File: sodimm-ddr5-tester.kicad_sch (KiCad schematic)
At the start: 2 parts

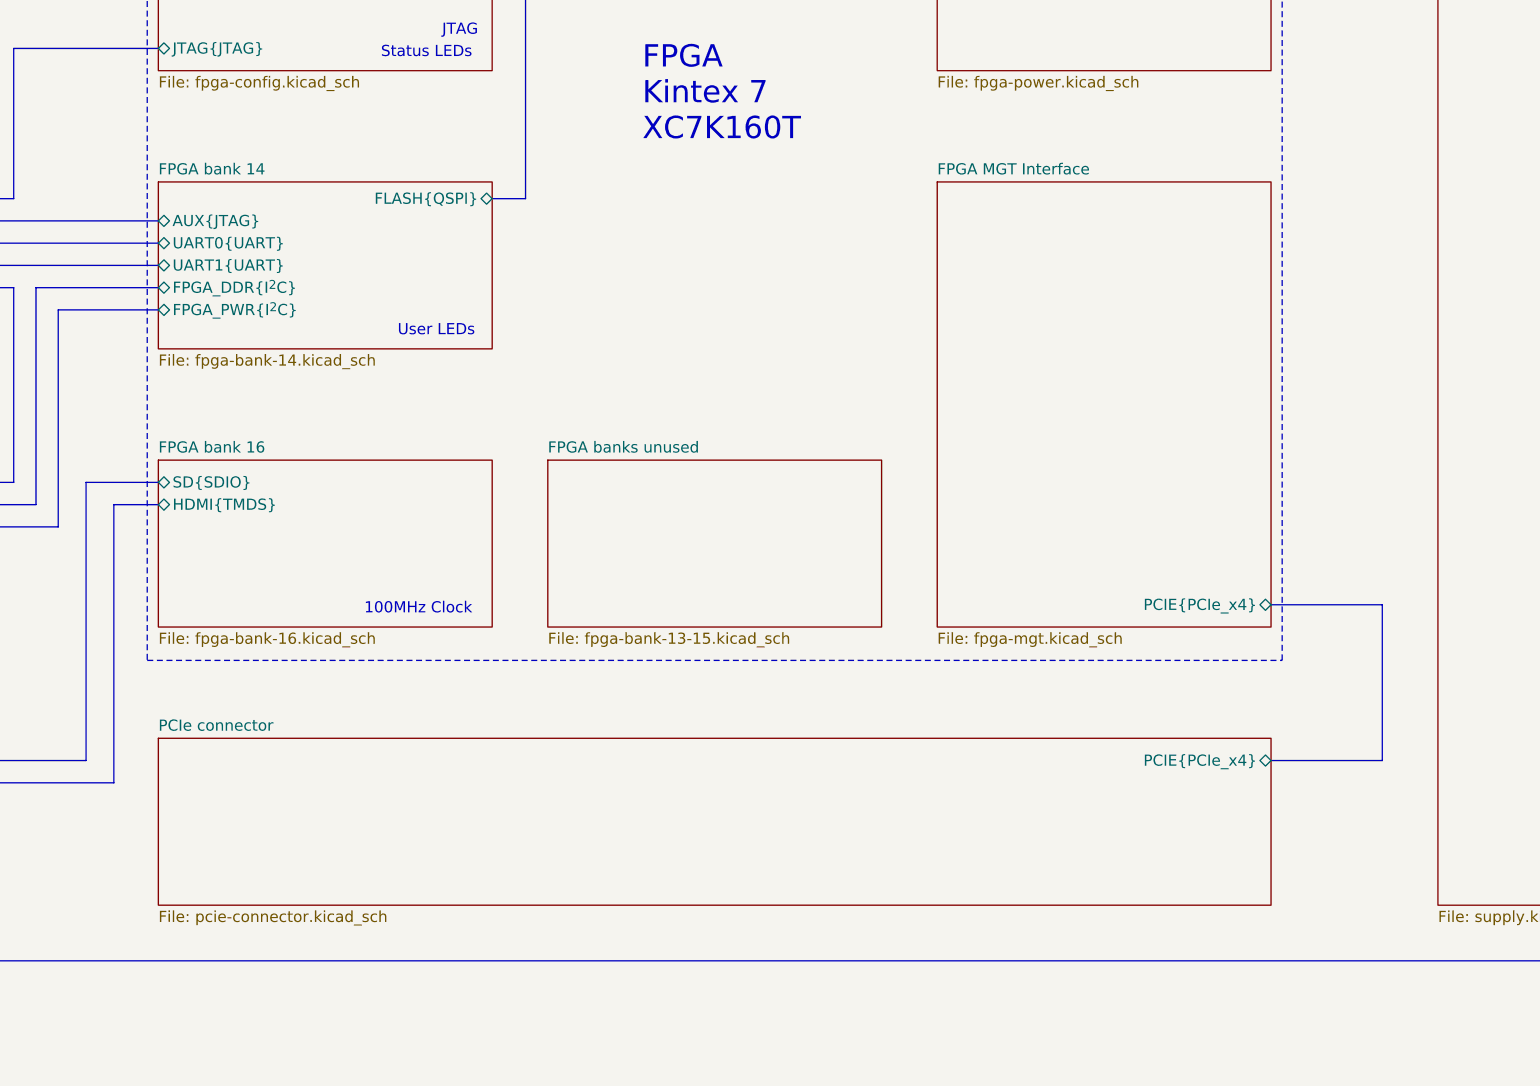
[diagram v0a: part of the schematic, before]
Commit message: Removing PCIe from sch and PCB
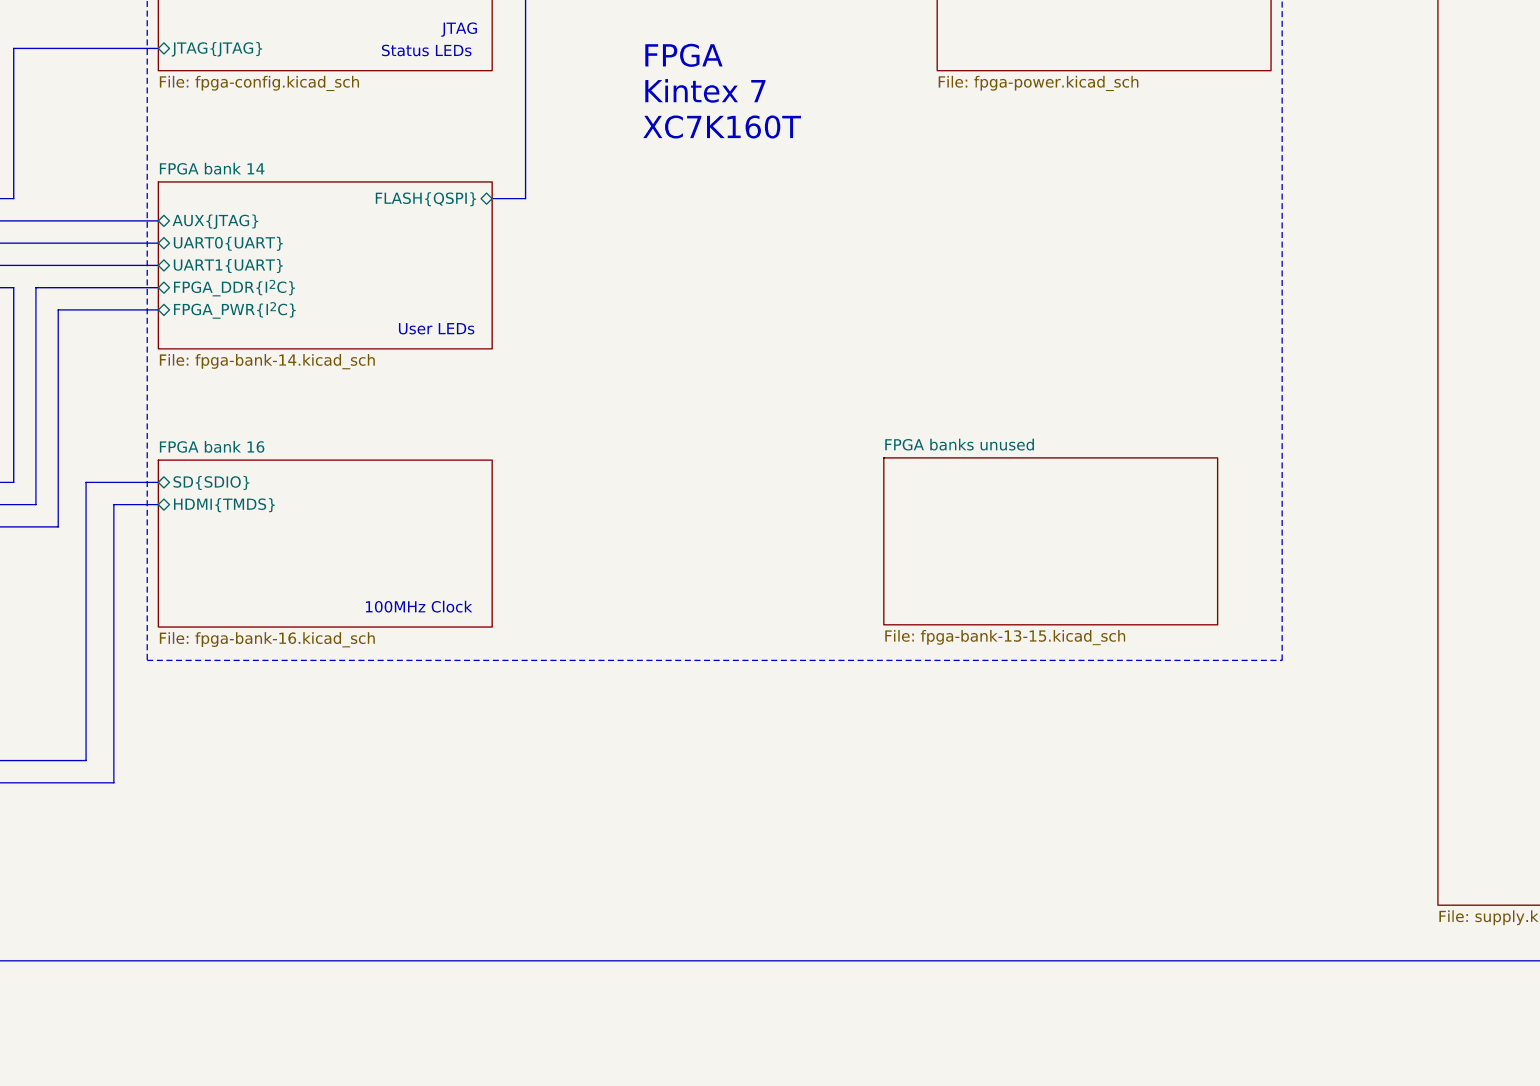
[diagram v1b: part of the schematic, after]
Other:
- removed sheet FPGA MGT Interface
- removed sheet PCIe connector
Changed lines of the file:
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@@
-    (stroke (width 0) (type default))
-  )
-  (bus (pts (xy 285.75 212.09) (xy 273.05 212.09))
     (stroke (width 0) (type default))
   )
@@
     (stroke (width 0) (type default))
   )
-  (bus (pts (xy 273.05 194.31) (xy 285.75 194.31))
-    (stroke (width 0) (type default))
-  )
   (bus (pts (xy 140.97 214.63) (xy 127 214.63))
     (stroke (width 0) (type default))
@@
   )
   (bus (pts (xy 281.94 62.865) (xy 273.05 62.865))
-    (stroke (width 0) (type default))
-  )
-  (bus (pts (xy 285.75 194.31) (xy 285.75 212.09))
     (stroke (width 0) (type default))
   )
@@
     )
   )
-  (sheet (at 190.5 177.8) (size 38.1 19.05) (fields_autoplaced)
+  (sheet (at 228.854 177.546) (size 38.1 19.05) (fields_autoplaced)
     (stroke (width 0.1524) (type solid))
     (fill (color 0 0 0 0.0000))
-    (property "Sheetname" "FPGA banks unused" (at 190.5 177.0884 0)
+    (property "Sheetname" "FPGA banks unused" (at 228.854 176.8344 0)
       (effects (font (size 1.27 1.27)) (justify left bottom))
     )
-    (property "Sheetfile" "fpga-bank-13-15.kicad_sch" (at 190.5 197.4346 0)
+    (property "Sheetfile" "fpga-bank-13-15.kicad_sch" (at 228.854 197.1806 0)
       (effects (font (size 1.27 1.27)) (justify left top))
     )
@@
       )
     )
-  )
-  (sheet (at 234.95 146.05) (size 38.1 50.8) (fields_autoplaced)
-    (stroke (width 0.1524) (type solid))
-    (fill (color 0 0 0 0.0000))
-    (property "Sheetname" "FPGA MGT Interface" (at 234.95 145.3384 0)
-      (effects (font (size 1.27 1.27)) (justify left bottom))
-    )
-    (property "Sheetfile" "fpga-mgt.kicad_sch" (at 234.95 197.4346 0)
-      (effects (font (size 1.27 1.27)) (justify left top))
-    )
-    (pin "PCIE{PCIe_x4}" bidirectional (at 273.05 194.31 0)
-      (effects (font (size 1.27 1.27)) (justify right))
-    )
-    (instances
-      (project "sodimm-ddr5-tester"
-        (path "/1faa6543-e26a-4449-8bac-ee14b9f19e5f" (page "11"))
-      )
-    )
-  )
-  (sheet (at 146.05 209.55) (size 127 19.05) (fields_autoplaced)
-    (stroke (width 0.1524) (type solid))
-    (fill (color 0 0 0 0.0000))
-    (property "Sheetname" "PCIe connector" (at 146.05 208.8384 0)
-      (effects (font (size 1.27 1.27)) (justify left bottom))
-    )
-    (property "Sheetfile" "pcie-connector.kicad_sch" (at 146.05 229.1846 0)
-      (effects (font (size 1.27 1.27)) (justify left top))
-    )
-    (pin "PCIE{PCIe_x4}" tri_state (at 273.05 212.09 0)
-      (effects (font (size 1.27 1.27)) (justify right))
-    )
-    (instances
-      (project "sodimm-ddr5-tester"
-        (path "/1faa6543-e26a-4449-8bac-ee14b9f19e5f" (page "12"))
-      )
-    )

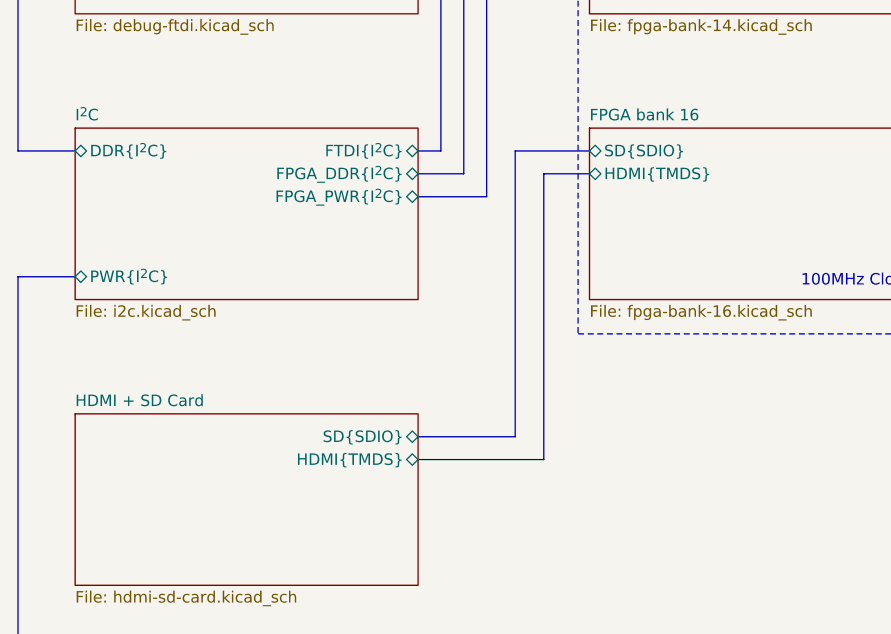
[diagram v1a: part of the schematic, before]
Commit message: Removing HDMI from sch and PCB
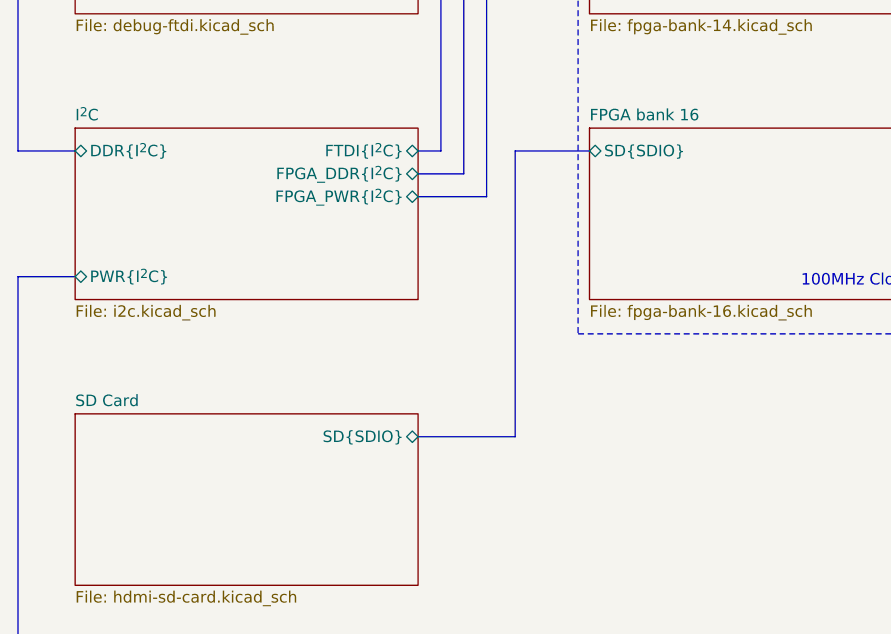
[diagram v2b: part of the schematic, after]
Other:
- sheet HDMI + SD Card renamed SD Card
- sheet FPGA bank 16 ports: added none; removed HDMI{TMDS}
- sheet SD Card ports: added none; removed HDMI{TMDS}
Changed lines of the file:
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@@
-    (stroke (width 0) (type default))
-  )
-  (bus (pts (xy 140.97 182.88) (xy 140.97 214.63))
-    (stroke (width 0) (type default))
-  )
-  (bus (pts (xy 146.05 182.88) (xy 140.97 182.88))
     (stroke (width 0) (type default))
   )
@@
   )
   (bus (pts (xy 127 158.115) (xy 129.54 158.115))
-    (stroke (width 0) (type default))
-  )
-  (bus (pts (xy 140.97 214.63) (xy 127 214.63))
     (stroke (width 0) (type default))
   )
@@
     (stroke (width 0.1524) (type solid))
     (fill (color 0 0 0 0.0000))
-    (property "Sheetname" "HDMI + SD Card" (at 88.9 208.8384 0)
+    (property "Sheetname" "SD Card" (at 88.9 208.8384 0)
       (effects (font (size 1.27 1.27)) (justify left bottom))
     )
     (property "Sheetfile" "hdmi-sd-card.kicad_sch" (at 88.9 229.1846 0)
       (effects (font (size 1.27 1.27)) (justify left top))
-    )
-    (pin "HDMI{TMDS}" bidirectional (at 127 214.63 0)
-      (effects (font (size 1.27 1.27)) (justify right))
     )
     (pin "SD{SDIO}" bidirectional (at 127 212.09 0)
@@
       (effects (font (size 1.27 1.27)) (justify left top))
     )
-    (pin "HDMI{TMDS}" bidirectional (at 146.05 182.88 180)
-      (effects (font (size 1.27 1.27)) (justify left))
-    )
     (pin "SD{SDIO}" bidirectional (at 146.05 180.34 180)
